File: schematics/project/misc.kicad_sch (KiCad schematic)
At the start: 0 parts

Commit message: First steps with kicad structure -> kinda sucks
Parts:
- added R?: R, Resistor_SMD:R_0603_1608Metric, symbol Device:R
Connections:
- net footpad_a : now also R?.1
- new net GND: R?.2
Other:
- note added: "- Footpad sensor zusätzlich/VORIGE eingänge (analog/digital) -2 bis 3 analoge eingänge für onboard poti - status leds - knopfbatterie - vlt signal hauptschalter - nfc chip für diebstahlschutz"
- note removed: "- Footpad sensor zusätzlich/VORIGE eingänge (analog/digital) -2 bis 3 analoge eingänge für onboard poti - vlt signal hauptschalter - nfc chip für diebstahlschutz"
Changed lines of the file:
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@@
 (kicad_sch (version 20211123) (generator eeschema)
   (paper "A4")
-  (text "- Footpad sensor\nzusätzlich/VORIGE eingänge (analog/digital)\n-2 bis 3 analoge eingänge für onboard poti\n\n- vlt signal hauptschalter\n- nfc chip für diebstahlschutz\n"
+  (junction (at 223.52 48.26) (diameter 0) (color 0 0 0 0)
+  )
+  (wire (pts (xy 223.52 48.26) (xy 223.52 52.07))
+    (stroke (width 0) (type default) (color 0 0 0 0))
+  )
+  (wire (pts (xy 209.55 48.26) (xy 223.52 48.26))
+    (stroke (width 0) (type default) (color 0 0 0 0))
+  )
+  (wire (pts (xy 209.55 41.91) (xy 223.52 41.91))
+    (stroke (width 0) (type default) (color 0 0 0 0))
+  )
+  (wire (pts (xy 223.52 38.1) (xy 223.52 41.91))
+    (stroke (width 0) (type default) (color 0 0 0 0))
+  )
+  (wire (pts (xy 223.52 48.26) (xy 232.41 48.26))
+    (stroke (width 0) (type default) (color 0 0 0 0))
+  )
+  (wire (pts (xy 223.52 59.69) (xy 223.52 62.23))
+    (stroke (width 0) (type default) (color 0 0 0 0))
+  )
+  (text "- Footpad sensor\nzusätzlich/VORIGE eingänge (analog/digital)\n-2 bis 3 analoge eingänge für onboard poti\n- status leds\n- knopfbatterie\n\n\n- vlt signal hauptschalter\n- nfc chip für diebstahlschutz\n"
     (at 124.46 55.88 0)
     (effects (font (size 1.27 1.27)) (justify left bottom))
   )
-  (hierarchical_label "footpad_a " (shape output) (at 167.64 69.85 0)
+  (hierarchical_label "footpad_a " (shape output) (at 232.41 48.26 0)
     (effects (font (size 1.27 1.27)) (justify left))
   )
+  (symbol (lib_id "power:+5V") (at 223.52 38.1 0) (unit 1)
+    (in_bom yes) (on_board yes) (fields_autoplaced)
+    (property "Reference" "#PWR?" (id 0) (at 223.52 41.91 0)
+      (effects (font (size 1.27 1.27)) hide)
+    )
+    (property "Value" "+5V" (id 1) (at 223.52 33.02 0))
+    (property "Footprint" "" (id 2) (at 223.52 38.1 0)
+      (effects (font (size 1.27 1.27)) hide)
+    )
+    (property "Datasheet" "" (id 3) (at 223.52 38.1 0)
+      (effects (font (size 1.27 1.27)) hide)
+    )
+    (pin "1")
+  )
+  (symbol (lib_id "power:GND") (at 223.52 62.23 0) (unit 1)
+    (in_bom yes) (on_board yes) (fields_autoplaced)
+    (property "Reference" "#PWR?" (id 0) (at 223.52 68.58 0)
+      (effects (font (size 1.27 1.27)) hide)
+    )
+    (property "Value" "GND" (id 1) (at 223.52 67.31 0))
+    (property "Footprint" "" (id 2) (at 223.52 62.23 0)
+      (effects (font (size 1.27 1.27)) hide)
+    )
+    (property "Datasheet" "" (id 3) (at 223.52 62.23 0)
+      (effects (font (size 1.27 1.27)) hide)
+    )
+    (pin "1")
+  )
+  (symbol (lib_id "Device:R") (at 223.52 55.88 0) (unit 1)
+    (in_bom yes) (on_board yes) (fields_autoplaced)
+    (property "Reference" "R?" (id 0) (at 226.06 54.6099 0)
+      (effects (font (size 1.27 1.27)) (justify left))
+    )
+    (property "Value" "R" (id 1) (at 226.06 57.1499 0)
+      (effects (font (size 1.27 1.27)) (justify left))
+    )
+    (property "Footprint" "Resistor_SMD:R_0603_1608Metric" (id 2) (at 221.742 55.88 90)
+      (effects (font (size 1.27 1.27)) hide)
+    )
+    (property "Datasheet" "~" (id 3) (at 223.52 55.88 0)
+      (effects (font (size 1.27 1.27)) hide)
+    )
+    (pin "1")
+    (pin "2")
+  )
 )

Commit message: some progress, dust slowly clears
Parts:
- gave numbers to parts that had none: 1
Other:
- note added: "- Footpad sensor zusätzlich/VORIGE eingänge (analog/digital) -2 bis 3 analoge eingänge für onboard poti - status leds - knopfbatterie - Speaker - vlt signal hauptschalter - nfc chip für diebstahlschutz"
- note removed: "- Footpad sensor zusätzlich/VORIGE eingänge (analog/digital) -2 bis 3 analoge eingänge für onboard poti - status leds - knopfbatterie - vlt signal hauptschalter - nfc chip für diebstahlschutz"
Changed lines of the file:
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@@
     (stroke (width 0) (type default) (color 0 0 0 0))
   )
-  (text "- Footpad sensor\nzusätzlich/VORIGE eingänge (analog/digital)\n-2 bis 3 analoge eingänge für onboard poti\n- status leds\n- knopfbatterie\n\n\n- vlt signal hauptschalter\n- nfc chip für diebstahlschutz\n"
+  (text "- Footpad sensor\nzusätzlich/VORIGE eingänge (analog/digital)\n-2 bis 3 analoge eingänge für onboard poti\n- status leds\n- knopfbatterie\n- Speaker\n\n\n- vlt signal hauptschalter\n- nfc chip für diebstahlschutz\n"
     (at 124.46 55.88 0)
     (effects (font (size 1.27 1.27)) (justify left bottom))
@@
   (symbol (lib_id "power:+5V") (at 223.52 38.1 0) (unit 1)
     (in_bom yes) (on_board yes) (fields_autoplaced)
-    (property "Reference" "#PWR?" (id 0) (at 223.52 41.91 0)
+    (property "Reference" "#PWR0136" (id 0) (at 223.52 41.91 0)
       (effects (font (size 1.27 1.27)) hide)
     )
@@
   (symbol (lib_id "power:GND") (at 223.52 62.23 0) (unit 1)
     (in_bom yes) (on_board yes) (fields_autoplaced)
-    (property "Reference" "#PWR?" (id 0) (at 223.52 68.58 0)
+    (property "Reference" "#PWR0137" (id 0) (at 223.52 68.58 0)
       (effects (font (size 1.27 1.27)) hide)
     )
@@
   (symbol (lib_id "Device:R") (at 223.52 55.88 0) (unit 1)
     (in_bom yes) (on_board yes) (fields_autoplaced)
-    (property "Reference" "R?" (id 0) (at 226.06 54.6099 0)
+    (property "Reference" "R13" (id 0) (at 226.06 54.6099 0)
       (effects (font (size 1.27 1.27)) (justify left))
     )

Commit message: small progress, angsthasen
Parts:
- added J3: Conn_01x06, symbol Connector_Generic:Conn_01x06
- added J4: Conn_01x02, symbol Connector_Generic:Conn_01x02
- added RV1, RV2, RV3: TC33X-1-203E, Potentiometer_SMD:Potentiometer_Bourns_TC33X_Vertical, symbol Device:R_Potentiometer
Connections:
- net +5V: now also J4.1 (Pin_1), RV1.1, RV2.1, RV3.1
- net GND: now also RV1.3, RV2.3, RV3.3
- net footpad_a : now also J4.2 (Pin_2)
- new net 5V_Speaker: J3.5 (Pin_5)
- new net AGND: J3.6 (Pin_6)
- new net AMP_EN: J3.3 (Pin_3)
- new net AudioIN: J3.4 (Pin_4)
- new net Speaker+: J3.1 (Pin_1)
- new net Speaker-: J3.2 (Pin_2)
- new net poti_IN_a0: RV1.2
- new net poti_IN_a1: RV2.2
- new net poti_IN_a2: RV3.2
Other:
- moved on the sheet: R13

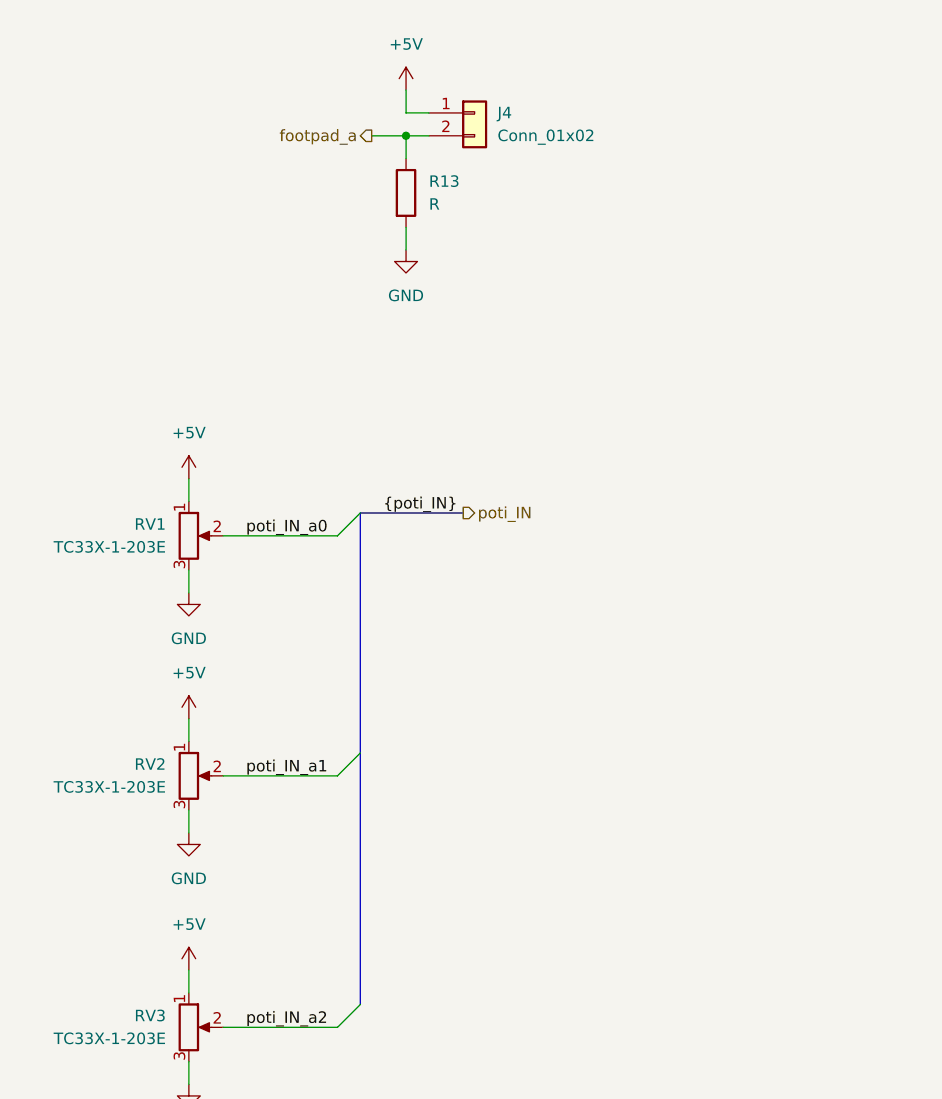
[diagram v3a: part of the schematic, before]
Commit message: Adding separate library, BT Module
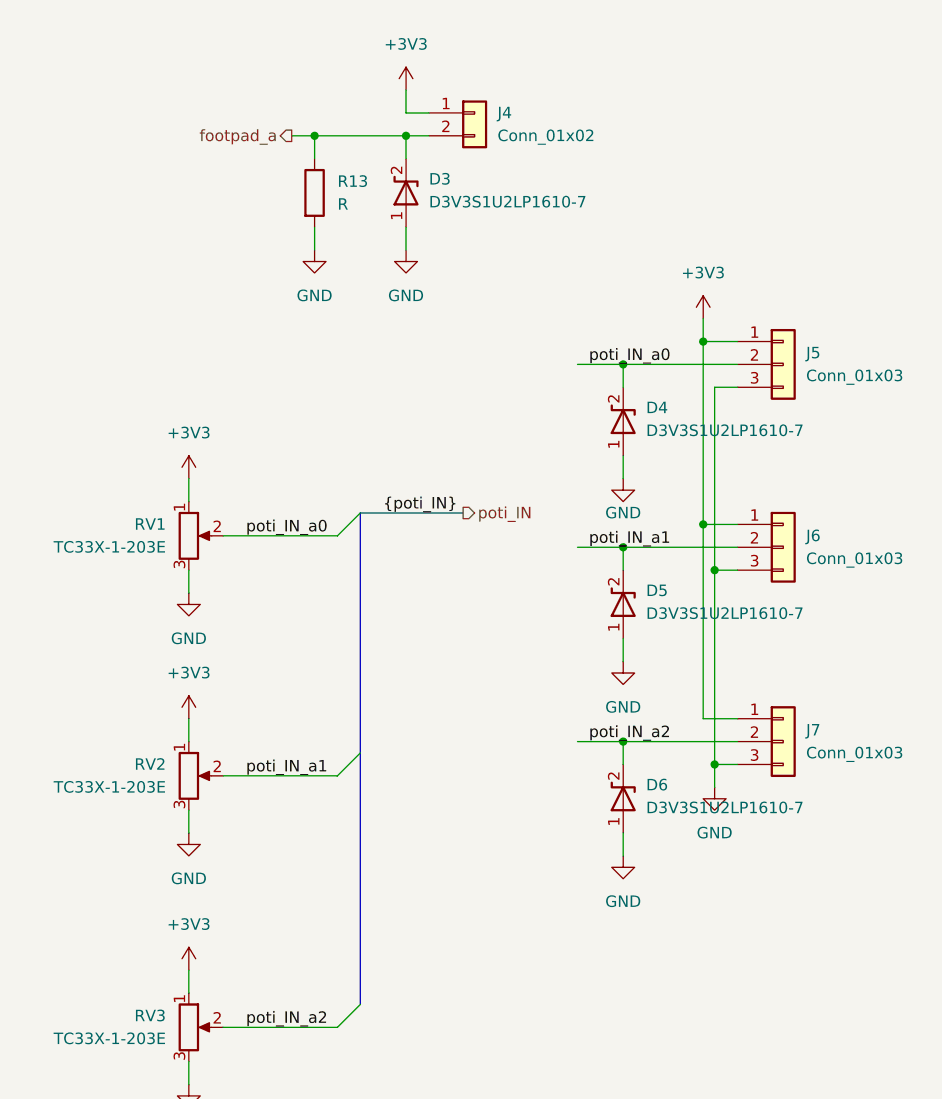
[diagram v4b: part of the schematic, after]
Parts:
- added D3, D4, D5, D6: D3V3S1U2LP1610-7, Diode_SMD:D_0603_1608Metric_Pad1.05x0.95mm_HandSolder, symbol IceWheelLib:D3V3S1U2LP1610-7
- added J5, J6, J7: Conn_01x03, symbol Connector_Generic:Conn_01x03
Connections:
- net GND: now also D3.1 (A1), D4.1 (A1), D5.1 (A1), D6.1 (A1), J5.3 (Pin_3), J6.3 (Pin_3), J7.3 (Pin_3)
- net footpad_a : now also D3.2 (A2)
- net poti_IN_a0: now also D4.2 (A2), J5.2 (Pin_2)
- net poti_IN_a1: now also D5.2 (A2), J6.2 (Pin_2)
- net poti_IN_a2: now also D6.2 (A2), J7.2 (Pin_2)
- net +5V renamed +3V3
- net +3V3: now also J5.1 (Pin_1), J6.1 (Pin_1), J7.1 (Pin_1)
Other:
- moved on the sheet: R13

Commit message: random commit
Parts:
- added D7, D8: D3V3S1U2LP1610-7, Diode_SMD:D_0603_1608Metric_Pad1.05x0.95mm_HandSolder, symbol IceWheelLib:D3V3S1U2LP1610-7
- J3: footprint (none) -> Connector_JST:JST_SH_SM06B-SRSS-TB_1x06-1MP_P1.00mm_Horizontal
- J4: footprint (none) -> Connector_JST:JST_SHL_SM02B-SHLS-TF_1x02-1MP_P1.00mm_Horizontal
- J5, J6, J7: footprint (none) -> Connector_JST:JST_SH_SM03B-SRSS-TB_1x03-1MP_P1.00mm_Horizontal
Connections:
- net GND: now also D7.1 (A1), D8.1 (A1)
- net Speaker+: now also D8.2 (A2)
- net Speaker-: now also D7.2 (A2)
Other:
- moved on the sheet: D3, J3, J4, R13, RV1, RV2, RV3
